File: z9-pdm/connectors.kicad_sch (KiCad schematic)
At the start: 11 parts, among them J10 RedCubeTerminal, J11 RedCubeTerminal, J12 Wago 12 pin 1 level 3.5mm 260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, J16 JST GH, J17 Wago 12 pin 1 level 3.5mm 260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, J19 Wago 12 pin 1 level 3.5mm 260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, J200 TE_DT15-12PC-B016 -Conn_01x12, J201 TE_DT15-12PC-B016 -Conn_01x12, J202 TE_DT15-12PC-B016 -Conn_01x12, J203 TE_DT15-12PC-B016 -Conn_01x12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

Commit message: connector routing
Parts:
- renumbered J17 to J12, J12 to J17, J203 to J202, J202 to J203
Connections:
- net +5V_ISO: now also J12.21 (11_1), J12.22 (11_2), J202.2 (Pin_2); no longer J12.13 (7_1), J12.14 (7_2), J202.7 (Pin_7)
- net +BATT: no longer J12.1 (1_1), J12.2 (1_2), J12.3 (2_1), J12.4 (2_2), J202.1 (Pin_1), J202.2 (Pin_2)
- net 5V_SENSOR_POWER: now also J12.13 (7_1), J12.14 (7_2), J202.6 (Pin_6); no longer J12.15 (8_1), J12.16 (8_2), J202.8 (Pin_8)
- net CAN_H: now also J202.9 (Pin_9); no longer J16.4, J202.4 (Pin_4)
- net CAN_L: now also J12.5 (3_1), J12.6 (3_2), J202.10 (Pin_10); no longer J12.10 (5_2), J12.9 (5_1), J16.5, J202.5 (Pin_5)
- net GND: now also J12.11 (6_1), J12.12 (6_2), J202.7 (Pin_7); no longer J12.5 (3_1), J12.6 (3_2), J202.3 (Pin_3)
- net GND_ISO: now also J12.10 (5_2), J12.9 (5_1), J202.8 (Pin_8); no longer J12.11 (6_1), J12.12 (6_2), J16.6, J202.6 (Pin_6)
- net SENSE_7: now also J12.15 (8_1), J12.16 (8_2), J202.5 (Pin_5); no longer J12.17 (9_1), J12.18 (9_2), J202.9 (Pin_9)
- net SENSE_8: now also J12.17 (9_1), J12.18 (9_2), J202.4 (Pin_4); no longer J12.19 (10_1), J12.20 (10_2), J202.10 (Pin_10)
- net SENSE_9: now also J12.19 (10_1), J12.20 (10_2), J202.3 (Pin_3); no longer J12.21 (11_1), J12.22 (11_2), J202.11 (Pin_11)
- net SENSE_GROUND: now also J202.1 (Pin_1); no longer J202.12 (Pin_12)
- new net +12V_VIPOWER: J12.1 (1_1), J12.2 (1_2), J12.3 (2_1), J12.4 (2_2), J202.11 (Pin_11), J202.12 (Pin_12)

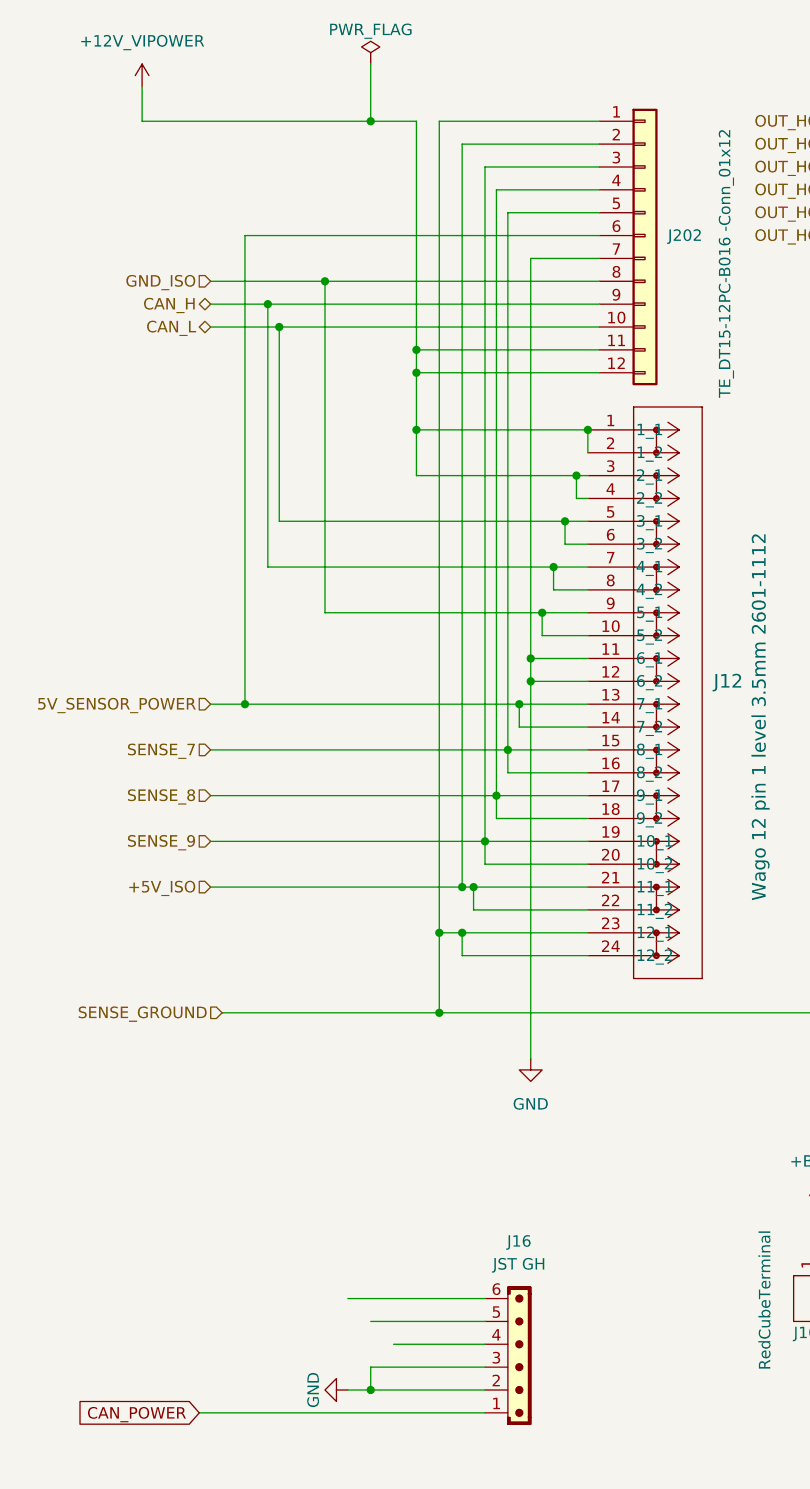
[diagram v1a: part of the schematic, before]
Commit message: Refactor junctions and wires in connectors schematic; remove unused labels and pins in z9-pdm schematic; update project settings to ignore four-way junction warnings; enhance ERC settings in shared project configuration.
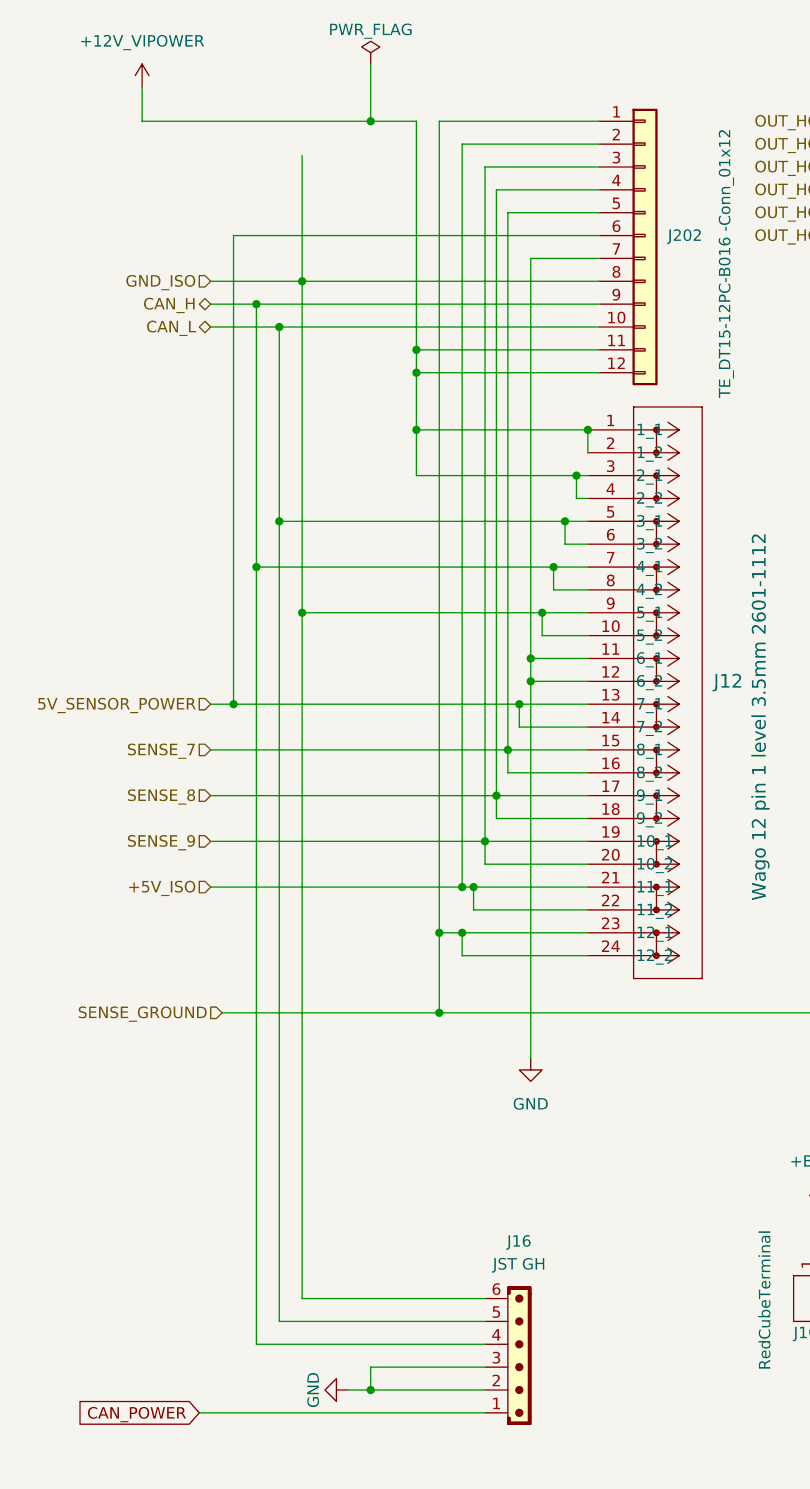
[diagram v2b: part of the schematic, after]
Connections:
- net CAN_H: now also J16.4
- net CAN_L: now also J16.5
- net GND_ISO: now also J16.6
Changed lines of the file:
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@@
+	)
+	(junction
+		(at 35.56 95.25)
+		(diameter 0)
+		(color 0 0 0 0)
 	)
 	(junction
@@
 	)
 	(junction
-		(at 36.83 95.25)
-		(diameter 0)
-		(color 0 0 0 0)
-	)
-	(junction
 		(at 176.53 115.57)
 		(diameter 0)
@@
 	)
 	(junction
+		(at 43.18 85.09)
+		(diameter 0)
+		(color 0 0 0 0)
+	)
+	(junction
 		(at 232.41 120.65)
 		(diameter 0)
@@
 	)
 	(junction
+		(at 43.18 48.26)
+		(diameter 0)
+		(color 0 0 0 0)
+	)
+	(junction
 		(at 104.14 48.26)
 		(diameter 0)
@@
 	)
 	(junction
+		(at 38.1 80.01)
+		(diameter 0)
+		(color 0 0 0 0)
+	)
+	(junction
 		(at 165.1 120.65)
 		(diameter 0)
@@
 	)
 	(junction
+		(at 40.64 74.93)
+		(diameter 0)
+		(color 0 0 0 0)
+	)
+	(junction
 		(at 179.07 40.64)
 		(diameter 0)
@@
 	)
 	(junction
-		(at 45.72 48.26)
-		(diameter 0)
-		(color 0 0 0 0)
-	)
-	(junction
 		(at 176.53 43.18)
 		(diameter 0)
@@
 	)
 	(junction
-		(at 39.37 50.8)
-		(diameter 0)
-		(color 0 0 0 0)
-	)
-	(junction
 		(at 165.1 50.8)
 		(diameter 0)
@@
 	)
 	(junction
+		(at 38.1 50.8)
+		(diameter 0)
+		(color 0 0 0 0)
+	)
+	(junction
 		(at 50.8 171.45)
 		(diameter 0)
@@
 	(wire
 		(pts
-			(xy 45.72 85.09) (xy 69.85 85.09)
+			(xy 38.1 166.37) (xy 63.5 166.37)
 		)
 		(stroke
@@
 	(wire
 		(pts
+			(xy 43.18 48.26) (xy 43.18 85.09)
+		)
+		(stroke
+			(width 0)
+			(type default)
+		)
+	)
+	(wire
+		(pts
 			(xy 232.41 69.85) (xy 232.41 80.01)
 		)
@@
 	(wire
 		(pts
-			(xy 39.37 80.01) (xy 71.12 80.01)
-		)
-		(stroke
-			(width 0)
-			(type default)
-		)
-	)
-	(wire
-		(pts
 			(xy 226.06 30.48) (xy 256.54 30.48)
 		)
@@
 	(wire
 		(pts
-			(xy 33.02 48.26) (xy 45.72 48.26)
+			(xy 33.02 48.26) (xy 43.18 48.26)
 		)
 		(stroke
@@
 	(wire
 		(pts
-			(xy 63.5 163.83) (xy 50.8 163.83)
-		)
-		(stroke
-			(width 0)
-			(type default)
-		)
-	)
-	(wire
-		(pts
 			(xy 33.02 53.34) (xy 40.64 53.34)
 		)
@@
 	(wire
 		(pts
+			(xy 35.56 95.25) (xy 67.31 95.25)
+		)
+		(stroke
+			(width 0)
+			(type default)
+		)
+	)
+	(wire
+		(pts
 			(xy 104.14 30.48) (xy 129.54 30.48)
 		)
@@
 	(wire
 		(pts
-			(xy 45.72 48.26) (xy 45.72 85.09)
-		)
-		(stroke
-			(width 0)
-			(type default)
-		)
-	)
-	(wire
-		(pts
 			(xy 104.14 100.33) (xy 129.54 100.33)
 		)
@@
 	(wire
 		(pts
-			(xy 36.83 43.18) (xy 76.2 43.18)
+			(xy 35.56 43.18) (xy 76.2 43.18)
+		)
+		(stroke
+			(width 0)
+			(type default)
+		)
+	)
+	(wire
+		(pts
+			(xy 38.1 80.01) (xy 71.12 80.01)
 		)
 		(stroke
@@
 	(wire
 		(pts
+			(xy 43.18 34.29) (xy 43.18 48.26)
+		)
+		(stroke
+			(width 0)
+			(type default)
+		)
+	)
+	(wire
+		(pts
 			(xy 124.46 85.09) (xy 124.46 87.63)
 		)
@@
 	(wire
 		(pts
-			(xy 36.83 43.18) (xy 36.83 95.25)
+			(xy 35.56 43.18) (xy 35.56 95.25)
 		)
 		(stroke
@@
 	(wire
 		(pts
-			(xy 63.5 166.37) (xy 53.34 166.37)
-		)
-		(stroke
-			(width 0)
-			(type default)
-		)
-	)
-	(wire
-		(pts
 			(xy 129.54 92.71) (xy 129.54 90.17)
 		)
@@
 	(wire
 		(pts
+			(xy 43.18 85.09) (xy 69.85 85.09)
+		)
+		(stroke
+			(width 0)
+			(type default)
+		)
+	)
+	(wire
+		(pts
 			(xy 189.23 30.48) (xy 189.23 64.77)
 		)
@@
 	(wire
 		(pts
+			(xy 40.64 163.83) (xy 40.64 74.93)
+		)
+		(stroke
+			(width 0)
+			(type default)
+		)
+	)
+	(wire
+		(pts
 			(xy 248.92 38.1) (xy 257.81 38.1)
 		)
@@
 	(wire
 		(pts
-			(xy 36.83 95.25) (xy 67.31 95.25)
-		)
-		(stroke
-			(width 0)
-			(type default)
-		)
-	)
-	(wire
-		(pts
 			(xy 179.07 40.64) (xy 161.29 40.64)
 		)
@@
 	(wire
 		(pts
+			(xy 43.18 85.09) (xy 43.18 161.29)
+		)
+		(stroke
+			(width 0)
+			(type default)
+		)
+	)
+	(wire
+		(pts
+			(xy 43.18 161.29) (xy 63.5 161.29)
+		)
+		(stroke
+			(width 0)
+			(type default)
+		)
+	)
+	(wire
+		(pts
 			(xy 25.4 26.67) (xy 25.4 30.48)
 		)
@@
 	(wire
 		(pts
-			(xy 45.72 48.26) (xy 76.2 48.26)
-		)
-		(stroke
-			(width 0)
-			(type default)
-		)
-	)
-	(wire
-		(pts
 			(xy 243.84 43.18) (xy 257.81 43.18)
 		)
@@
 	(wire
 		(pts
-			(xy 39.37 50.8) (xy 76.2 50.8)
-		)
-		(stroke
-			(width 0)
-			(type default)
-		)
-	)
-	(wire
-		(pts
 			(xy 55.88 64.77) (xy 55.88 69.85)
 		)
@@
 	(wire
 		(pts
+			(xy 38.1 50.8) (xy 38.1 80.01)
+		)
+		(stroke
+			(width 0)
+			(type default)
+		)
+	)
+	(wire
+		(pts
 			(xy 232.41 45.72) (xy 232.41 48.26)
 		)
@@
 	(wire
 		(pts
+			(xy 40.64 163.83) (xy 63.5 163.83)
+		)
+		(stroke
+			(width 0)
+			(type default)
+		)
+	)
+	(wire
+		(pts
 			(xy 119.38 40.64) (xy 119.38 105.41)
 		)
@@
 	(wire
 		(pts
-			(xy 39.37 50.8) (xy 39.37 80.01)
-		)
-		(stroke
-			(width 0)
-			(type default)
-		)
-	)
-	(wire
-		(pts
 			(xy 184.15 35.56) (xy 184.15 85.09)
 		)
@@
 	(wire
 		(pts
+			(xy 38.1 50.8) (xy 76.2 50.8)
+		)
+		(stroke
+			(width 0)
+			(type default)
+		)
+	)
+	(wire
+		(pts
 			(xy 232.41 53.34) (xy 232.41 55.88)
 		)
@@
 	(wire
 		(pts
-			(xy 33.02 50.8) (xy 39.37 50.8)
+			(xy 33.02 50.8) (xy 38.1 50.8)
 		)
 		(stroke
@@
 	(wire
 		(pts
-			(xy 33.02 95.25) (xy 36.83 95.25)
+			(xy 38.1 80.01) (xy 38.1 166.37)
+		)
+		(stroke
+			(width 0)
+			(type default)
+		)
+	)
+	(wire
+		(pts
+			(xy 33.02 95.25) (xy 35.56 95.25)
 		)
 		(stroke
@@
 	(wire
 		(pts
-			(xy 63.5 161.29) (xy 48.26 161.29)
-		)
-		(stroke
-			(width 0)
-			(type default)
-		)
-	)
-	(wire
-		(pts
 			(xy 104.14 110.49) (xy 104.14 120.65)
 		)
@@
 		)
 		(stroke
+			(width 0)
+			(type default)
+		)
+	)
+	(wire
+		(pts
+			(xy 43.18 48.26) (xy 76.2 48.26)
+		)
+		(stroke
